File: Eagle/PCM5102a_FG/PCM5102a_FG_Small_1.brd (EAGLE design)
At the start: 70.8 x 66 mm, 28 parts, among them IC1 PSOC_5LP_PROTOTIYPING_KIT, IC2 PCM5102A, IC3 TA48M033F, Q1 20MHz

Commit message: Update: Eagle Files
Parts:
- moved C6 3.59 mm to (47.0, 15.2)
- moved C15 3.59 mm to (25.4, 21.6)
- moved C1 2.54 mm to (35.6, 58.4)
- moved C11 2.54 mm to (17.8, 57.1)
- moved C2 2.54 mm to (45.7, 58.4)
- moved C5 2.54 mm to (38.1, 21.6)
- moved IC1 2.54 mm to (34.3, 41.9)
- moved JP1 2.54 mm to (61.0, 58.4)
- moved JP2 2.54 mm to (25.4, 58.4)
- moved Q1 2.54 mm to (40.6, 55.9)
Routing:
- net DGND: track 0.00 -> 225.6 mm
- net +3V3: track 0.00 -> 138.4 mm
- net AGND: track 0.00 -> 56.1 mm
- net I2C_SW: track 0.00 -> 50.4 mm
- net N$6: track 0.00 -> 22.9 mm
- net N$7: track 0.00 -> 20.3 mm
- net DC4.5V: track 0.00 -> 17.8 mm
- net N$18: track 0.00 -> 14.8 mm
- net N$2: track 0.00 -> 12.7 mm
- net N$4: track 0.00 -> 12.3 mm
- net N$9: track 0.00 -> 7.62 mm
- net N$8: track 0.00 -> 7.62 mm
- net N$15: track 0.00 -> 7.62 mm
- net N$14: track 0.00 -> 7.62 mm
- net N$13: track 0.00 -> 7.62 mm
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
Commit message: 電源電圧測定
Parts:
- added R4, R5: 100k, resistor:0207/7
- moved C1 2.54 mm to (33.0, 58.4), turned to 90 degrees
- moved C2 2.54 mm to (48.3, 58.4), turned to 90 degrees
- moved Q1 2.54 mm to (40.6, 58.4)
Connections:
- new net N$19: IC1.45, R4.2, R5.1
- net +3V3: now also R5.2
- net DGND: now also R4.1
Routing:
- net N$19: track 0.00 -> 26.5 mm
- net N$17: track 7.62 -> 15.2 mm
- net N$16: track 5.33 -> 10.3 mm
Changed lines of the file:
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@@
 </autorouter>
 <elements>
-<element name="C1" library="rcl" package="C050-024X044" value="22pF" x="35.56" y="58.42" rot="R180"/>
+<element name="C1" library="rcl" package="C050-024X044" value="22pF" x="33.02" y="58.42" rot="R90"/>
 <element name="C10" library="rcl" package="C050-035X075" value="2200p" x="58.42" y="5.08" rot="R270"/>
 <element name="C11" library="rcl" package="E2,5-5" value="10uF" x="17.78" y="57.15" rot="R270"/>
@@
 <element name="C15" library="rcl" package="E2,5-7" value="100uF" x="25.4" y="21.59" rot="R90"/>
 <element name="C16" library="rcl" package="E2,5-5" value="10uF" x="38.1" y="11.43" rot="R270"/>
-<element name="C2" library="rcl" package="C050-024X044" value="22pF" x="45.72" y="58.42"/>
+<element name="C2" library="rcl" package="C050-024X044" value="22pF" x="48.26" y="58.42" rot="R90"/>
 <element name="C3" library="rcl" package="C025-024X044" value="0.1uF" x="44.45" y="25.4" rot="R180"/>
 <element name="C4" library="rcl" package="C025-024X044" value="0.1uF" x="48.26" y="24.13" rot="R270"/>
@@
 <element name="JP5" library="pinhead" package="1X02" value="DC4.5V" x="11.43" y="7.62"/>
 <element name="LED1" library="led" package="LED3MM" value="BLUE" x="5.08" y="19.05" rot="R90"/>
-<element name="Q1" library="crystal" package="HC49/S" value="20MHz" x="40.64" y="55.88" rot="R180">
-<attribute name="OC_NEWARK" value="unknown" x="40.64" y="55.88" size="1.778" layer="27" rot="R180" display="off"/>
-<attribute name="MPN" value="" x="40.64" y="55.88" size="1.778" layer="27" rot="R180" display="off"/>
-<attribute name="MF" value="" x="40.64" y="55.88" size="1.778" layer="27" rot="R180" display="off"/>
-<attribute name="OC_FARNELL" value="1667008" x="40.64" y="55.88" size="1.778" layer="27" rot="R180" display="off"/>
+<element name="Q1" library="crystal" package="HC49/S" value="20MHz" x="40.64" y="58.42" rot="R180">
+<attribute name="OC_NEWARK" value="unknown" x="40.64" y="58.42" size="1.778" layer="27" rot="R180" display="off"/>
+<attribute name="MPN" value="" x="40.64" y="58.42" size="1.778" layer="27" rot="R180" display="off"/>
+<attribute name="MF" value="" x="40.64" y="58.42" size="1.778" layer="27" rot="R180" display="off"/>
+<attribute name="OC_FARNELL" value="1667008" x="40.64" y="58.42" size="1.778" layer="27" rot="R180" display="off"/>
 </element>
 <element name="R1" library="rcl" package="0207/7" value="470" x="64.77" y="2.54" rot="R180"/>
 <element name="R2" library="resistor" package="0207/7" value="0" x="68.58" y="16.51" rot="R270"/>
 <element name="R3" library="resistor" package="0207/7" value="1k" x="5.08" y="11.43" rot="R270"/>
+<element name="R4" library="resistor" package="0207/7" value="100k" x="29.21" y="27.94"/>
+<element name="R5" library="resistor" package="0207/7" value="100k" x="33.02" y="21.59" rot="R270"/>
 </elements>
 <signals>
@@
 <wire x1="5.08" y1="53.34" x2="5.08" y2="55.88" width="0.4064" layer="16"/>
 <wire x1="5.08" y1="55.88" x2="17.78" y2="55.88" width="0.4064" layer="16"/>
-<wire x1="22.86" y1="58.42" x2="22.86" y2="60.96" width="0.4064" layer="16"/>
-<wire x1="22.86" y1="60.96" x2="33.02" y2="60.96" width="0.4064" layer="16"/>
-<wire x1="33.02" y1="60.96" x2="48.26" y2="60.96" width="0.4064" layer="16"/>
-<wire x1="48.26" y1="60.96" x2="48.26" y2="58.42" width="0.4064" layer="16"/>
-<wire x1="33.02" y1="58.42" x2="33.02" y2="60.96" width="0.4064" layer="16"/>
 <wire x1="45.72" y1="27.94" x2="45.72" y2="25.4" width="0.4064" layer="16"/>
-<wire x1="48.26" y1="60.96" x2="68.58" y2="60.96" width="0.4064" layer="16"/>
 <wire x1="68.58" y1="60.96" x2="68.58" y2="58.42" width="0.4064" layer="16"/>
 <wire x1="68.58" y1="58.42" x2="68.58" y2="30.48" width="0.4064" layer="16"/>
@@
 <wire x1="11.43" y1="21.59" x2="12.7" y2="20.32" width="0.4064" layer="1"/>
 <wire x1="66.04" y1="58.42" x2="68.58" y2="58.42" width="0.4064" layer="16"/>
+<contactref element="R4" pad="1"/>
+<wire x1="25.4" y1="27.94" x2="25.4" y2="22.86" width="0.4064" layer="16"/>
+<wire x1="22.86" y1="58.42" x2="22.86" y2="60.96" width="0.4064" layer="16"/>
+<wire x1="22.86" y1="60.96" x2="33.02" y2="60.96" width="0.4064" layer="16"/>
+<wire x1="33.02" y1="60.96" x2="48.26" y2="60.96" width="0.4064" layer="16"/>
+<wire x1="48.26" y1="60.96" x2="68.58" y2="60.96" width="0.4064" layer="16"/>
 </signal>
 <signal name="N$1">
@@
 <wire x1="15.24" y1="20.32" x2="15.24" y2="17.78" width="0.4064" layer="16"/>
 <wire x1="25.4" y1="20.32" x2="30.48" y2="20.32" width="0.4064" layer="16"/>
-<wire x1="30.48" y1="20.32" x2="38.1" y2="12.7" width="0.4064" layer="16"/>
 <wire x1="38.1" y1="12.7" x2="43.18" y2="12.7" width="0.4064" layer="16"/>
 <wire x1="50.8" y1="27.94" x2="50.8" y2="17.78" width="0.4064" layer="16"/>
@@
 <wire x1="49.53" y1="31.75" x2="50.8" y2="30.48" width="0.4064" layer="1"/>
 <wire x1="50.8" y1="30.48" x2="50.8" y2="27.94" width="0.4064" layer="1"/>
+<contactref element="R5" pad="2"/>
+<wire x1="33.02" y1="17.78" x2="30.48" y2="20.32" width="0.4064" layer="16"/>
+<wire x1="33.02" y1="17.78" x2="38.1" y2="12.7" width="0.4064" layer="16"/>
 </signal>
 <signal name="N$2">
@@
 <contactref element="Q1" pad="2"/>
 <contactref element="C1" pad="1"/>
-<wire x1="40.64" y1="53.34" x2="40.64" y2="55.88" width="0.4064" layer="16"/>
-<wire x1="40.64" y1="55.88" x2="38.227" y2="55.88" width="0.4064" layer="16"/>
-<wire x1="38.227" y1="55.88" x2="38.1" y2="55.88" width="0.4064" layer="16"/>
-<wire x1="38.1" y1="55.88" x2="38.1" y2="58.42" width="0.4064" layer="16"/>
+<wire x1="33.02" y1="55.88" x2="33.02" y2="58.42" width="0.4064" layer="16"/>
+<wire x1="33.02" y1="58.42" x2="38.227" y2="58.42" width="0.4064" layer="16"/>
+<wire x1="38.227" y1="58.42" x2="40.64" y2="58.42" width="0.4064" layer="16"/>
+<wire x1="40.64" y1="58.42" x2="40.64" y2="53.34" width="0.4064" layer="16"/>
 </signal>
 <signal name="RE_A">
@@
 <contactref element="IC1" pad="10"/>
 <contactref element="C2" pad="1"/>
-<wire x1="43.18" y1="53.34" x2="43.053" y2="53.34" width="0.4064" layer="16"/>
-<wire x1="43.053" y1="53.34" x2="43.053" y2="55.88" width="0.4064" layer="16"/>
-<wire x1="43.053" y1="55.88" x2="43.18" y2="55.88" width="0.4064" layer="16"/>
-<wire x1="43.18" y1="55.88" x2="43.18" y2="58.42" width="0.4064" layer="16"/>
+<wire x1="43.053" y1="58.42" x2="43.053" y2="55.88" width="0.4064" layer="16"/>
+<wire x1="43.053" y1="55.88" x2="43.053" y2="53.467" width="0.4064" layer="16"/>
+<wire x1="43.053" y1="53.467" x2="43.18" y2="53.34" width="0.4064" layer="16"/>
+<wire x1="48.26" y1="55.88" x2="43.053" y2="55.88" width="0.4064" layer="16"/>
 </signal>
 <signal name="N$18">
@@
 <wire x1="68.58" y1="27.94" x2="63.5" y2="33.02" width="0.4064" layer="1"/>
 </signal>
+<signal name="N$19">
+<contactref element="R4" pad="2"/>
+<contactref element="R5" pad="1"/>
+<contactref element="IC1" pad="45"/>
+<wire x1="33.02" y1="27.94" x2="33.02" y2="25.4" width="0.4064" layer="16"/>
+<wire x1="33.02" y1="27.94" x2="33.02" y2="30.48" width="0.4064" layer="1"/>
+<wire x1="33.02" y1="30.48" x2="34.29" y2="31.75" width="0.4064" layer="1"/>
+<wire x1="34.29" y1="31.75" x2="34.29" y2="34.29" width="0.4064" layer="1"/>
+<wire x1="34.29" y1="34.29" x2="35.56" y2="35.56" width="0.4064" layer="1"/>
+<wire x1="35.56" y1="35.56" x2="48.26" y2="35.56" width="0.4064" layer="1"/>
+<wire x1="48.26" y1="35.56" x2="48.26" y2="33.02" width="0.4064" layer="1"/>
+</signal>
 </signals>

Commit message: LCDのコントラスト調整
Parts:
- R3: value 1k -> 4.7k
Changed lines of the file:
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@@
 <element name="R1" library="rcl" package="0207/7" value="470" x="64.77" y="2.54" rot="R180"/>
 <element name="R2" library="resistor" package="0207/7" value="0" x="68.58" y="16.51" rot="R270"/>
-<element name="R3" library="resistor" package="0207/7" value="1k" x="5.08" y="11.43" rot="R270"/>
+<element name="R3" library="resistor" package="0207/7" value="4.7k" x="5.08" y="11.43" rot="R270"/>
 <element name="R4" library="resistor" package="0207/7" value="100k" x="29.21" y="27.94"/>
 <element name="R5" library="resistor" package="0207/7" value="100k" x="33.02" y="21.59" rot="R270"/>

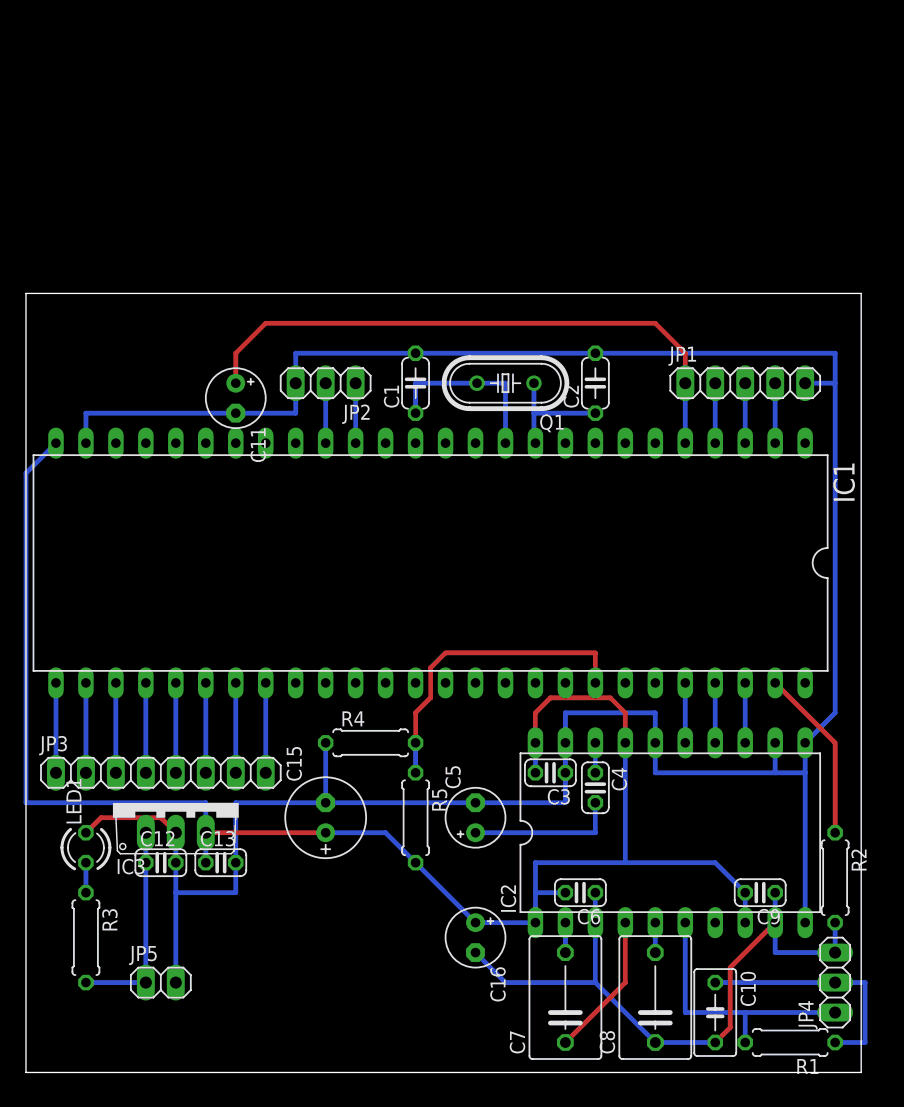
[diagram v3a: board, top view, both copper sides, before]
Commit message: 基板図修正: PCM5102a_FG_Small_1.sch/brd
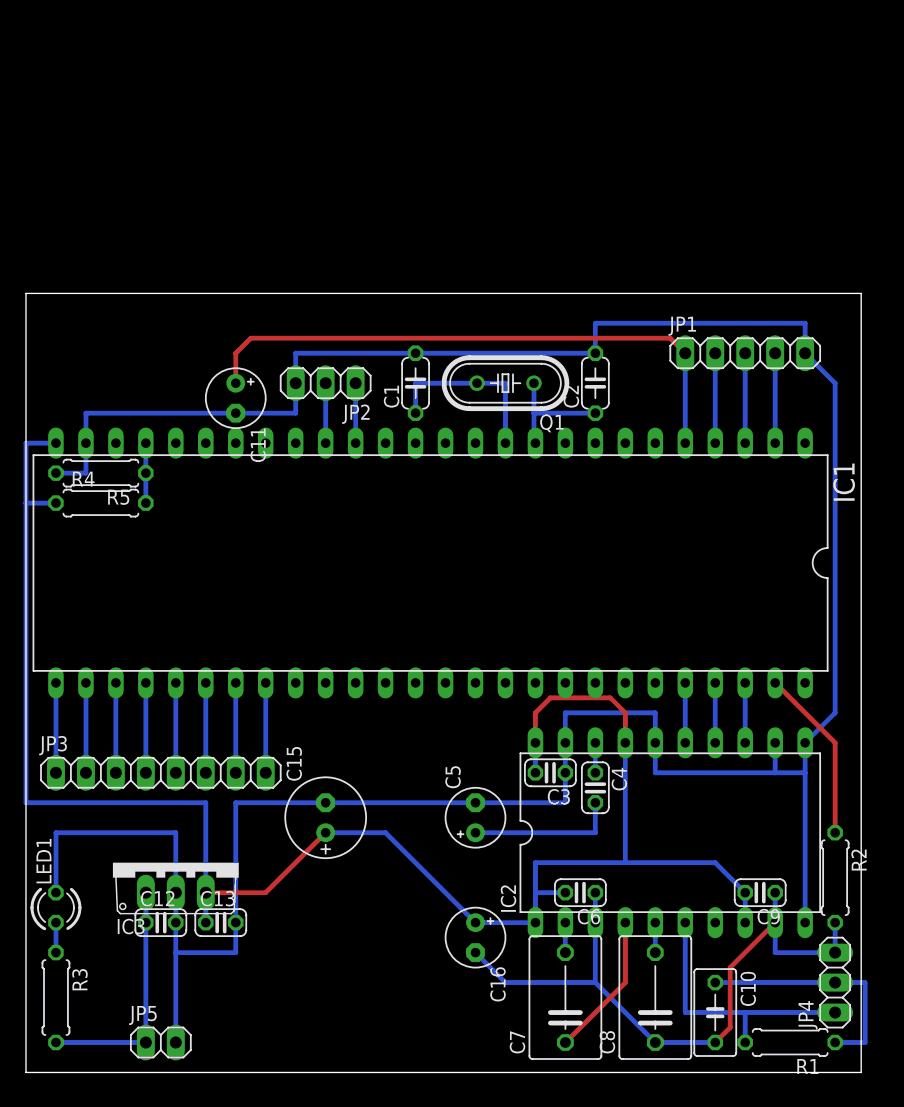
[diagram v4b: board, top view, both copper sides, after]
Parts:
- moved R5 39.6 mm to (6.35, 50.8), turned to 180 degrees
- moved R4 30.6 mm to (6.35, 48.3)
- moved LED1 5.68 mm to (2.54, 14.0)
- moved R3 5.68 mm to (2.54, 6.35)
- moved C12 5.08 mm to (11.4, 12.7)
- moved C13 5.08 mm to (16.5, 12.7)
- moved JP5 5.08 mm to (11.4, 2.54)
- moved IC3 5.08 mm to (12.7, 17.8)
- moved JP1 2.54 mm to (61.0, 61.0)
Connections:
- net +3V3: now also R4.1; no longer R5.2
- net DGND: now also R5.2; no longer R4.1
- net N$19: now also IC1.23; no longer IC1.45
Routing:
- net N$19: track 26.5 -> 5.08 mm
- net DGND: track 225.6 -> 243.4 mm
- net +3V3: track 138.4 -> 149.6 mm
- net I2C_SDA: track 5.08 -> 7.62 mm
- net I2C_SCL: track 5.08 -> 7.62 mm
- net I2C_RST: track 5.08 -> 7.62 mm
- net DC4.5V: track 17.8 -> 20.3 mm
- net I2C_SW: track 50.4 -> 49.3 mm

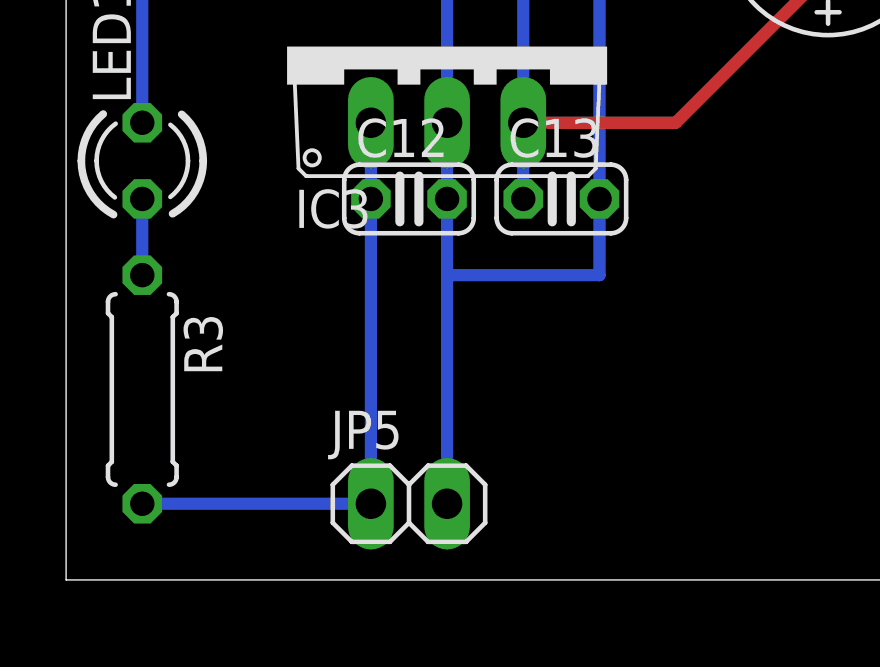
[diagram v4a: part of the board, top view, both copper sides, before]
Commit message: PCM5102a_FG_Small_1.sch/brd Add: SBD
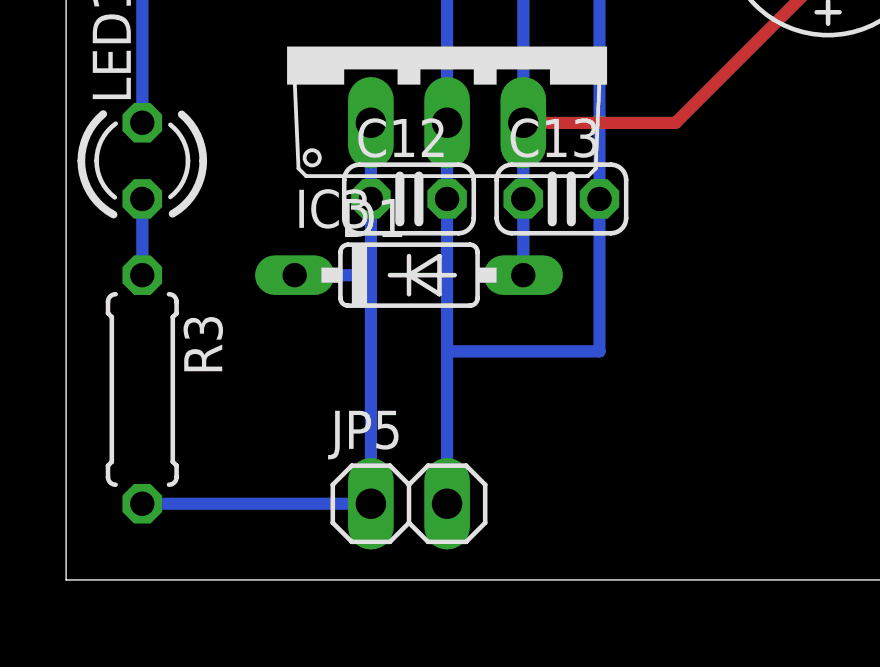
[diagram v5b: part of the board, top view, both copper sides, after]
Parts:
- added D1: 1S4, diode:DO35-7
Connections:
- net +3V3: now also D1.A
- net DC4.5V: now also D1.C
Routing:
- net DGND: track 243.4 -> 245.9 mm
- net DC4.5V: track 20.3 -> 22.9 mm
- net +3V3: track 149.6 -> 152.1 mm
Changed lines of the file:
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@@
 <element name="R4" library="resistor" package="0207/7" value="100k" x="6.35" y="48.26"/>
 <element name="R5" library="resistor" package="0207/7" value="100k" x="6.35" y="50.8" rot="R180"/>
+<element name="D1" library="diode" package="DO35-7" value="1S4" x="11.43" y="10.16"/>
 </elements>
 <signals>
@@
 <wire x1="45.72" y1="30.48" x2="45.72" y2="27.94" width="0.4064" layer="16"/>
 <wire x1="12.7" y1="12.7" x2="12.7" y2="15.24" width="0.4064" layer="16"/>
-<wire x1="12.7" y1="10.16" x2="17.78" y2="10.16" width="0.4064" layer="16"/>
-<wire x1="17.78" y1="10.16" x2="17.78" y2="12.7" width="0.4064" layer="16"/>
-<wire x1="12.7" y1="2.54" x2="12.7" y2="10.16" width="0.4064" layer="16"/>
-<wire x1="12.7" y1="10.16" x2="12.7" y2="12.7" width="0.4064" layer="16"/>
+<wire x1="12.7" y1="7.62" x2="17.78" y2="7.62" width="0.4064" layer="16"/>
+<wire x1="17.78" y1="7.62" x2="17.78" y2="12.7" width="0.4064" layer="16"/>
+<wire x1="12.7" y1="2.54" x2="12.7" y2="7.62" width="0.4064" layer="16"/>
+<wire x1="12.7" y1="7.62" x2="12.7" y2="12.7" width="0.4064" layer="16"/>
 <wire x1="66.04" y1="12.7" x2="66.04" y2="25.4" width="0.4064" layer="16"/>
 <wire x1="66.04" y1="25.4" x2="66.04" y2="27.94" width="0.4064" layer="16"/>
@@
 <wire x1="15.24" y1="15.24" x2="20.32" y2="15.24" width="0.4064" layer="1"/>
 <wire x1="20.32" y1="15.24" x2="25.4" y2="20.32" width="0.4064" layer="1"/>
+<contactref element="D1" pad="A"/>
+<wire x1="15.24" y1="10.16" x2="15.24" y2="12.7" width="0.4064" layer="16"/>
 </signal>
 <signal name="N$2">
@@
 <contactref element="R3" pad="2"/>
 <wire x1="10.16" y1="15.24" x2="10.16" y2="12.7" width="0.4064" layer="16"/>
-<wire x1="10.16" y1="12.7" x2="10.16" y2="2.54" width="0.4064" layer="16"/>
+<wire x1="10.16" y1="12.7" x2="10.16" y2="10.16" width="0.4064" layer="16"/>
+<wire x1="10.16" y1="10.16" x2="10.16" y2="2.54" width="0.4064" layer="16"/>
 <wire x1="2.54" y1="2.54" x2="10.16" y2="2.54" width="0.4064" layer="16"/>
+<contactref element="D1" pad="C"/>
+<wire x1="7.62" y1="10.16" x2="10.16" y2="10.16" width="0.4064" layer="16"/>
 </signal>
 <signal name="N$20">
